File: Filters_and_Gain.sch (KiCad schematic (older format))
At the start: 24 parts, among them U4 OPA388, U5 OPA388, U6 OPA388

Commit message: #4 - Routed board
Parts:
- removed TP18: TestPoint, TestPoint:TestPoint_Pad_D2.0mm, symbol Connector:TestPoint
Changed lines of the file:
@@
 $EndComp
 Connection ~ 5625 3025
-Wire Wire Line
-	5625 1450 5625 1775
 Connection ~ 5625 2300
 Wire Wire Line
@@
 	3175 2200 3575 2200
 $Comp
-L Connector:TestPoint TP18
-U 1 1 5FCA32EA
-P 5625 1775
-F 0 "TP18" V 5579 1963 50  0000 L CNN
-F 1 "TestPoint" V 5670 1963 50  0000 L CNN
-F 2 "TestPoint:TestPoint_Pad_D2.0mm" H 5825 1775 50  0001 C CNN
-F 3 "~" H 5825 1775 50  0001 C CNN
-	1    5625 1775
-	0    1    1    0
-$EndComp
-Connection ~ 5625 1775
-Wire Wire Line
-	5625 1775 5625 2300
-$Comp
 L Device:C C20
 U 1 1 5FCDCCC4
@@
 Wire Wire Line
 	5625 2300 5625 2725
+Wire Wire Line
+	5625 1450 5625 2300
 $EndSCHEMATC

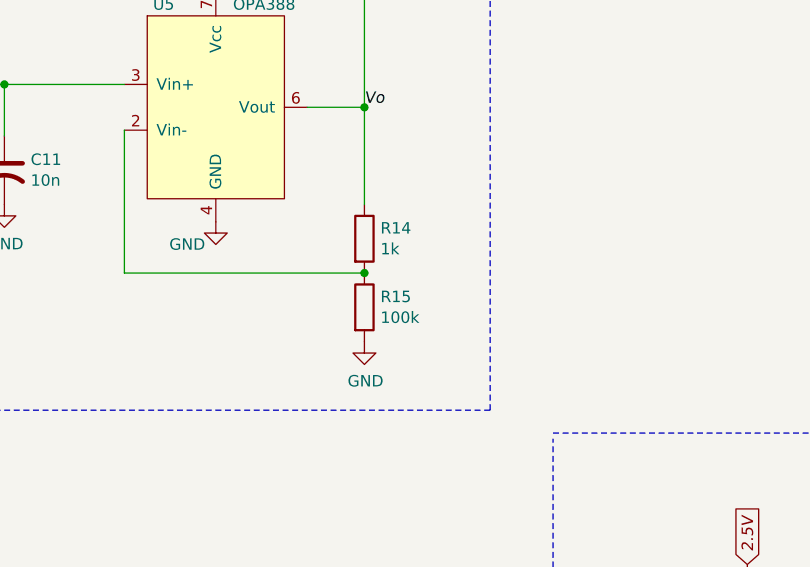
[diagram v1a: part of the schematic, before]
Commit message: #24 - Flip PNP and update low pass filter output resistors
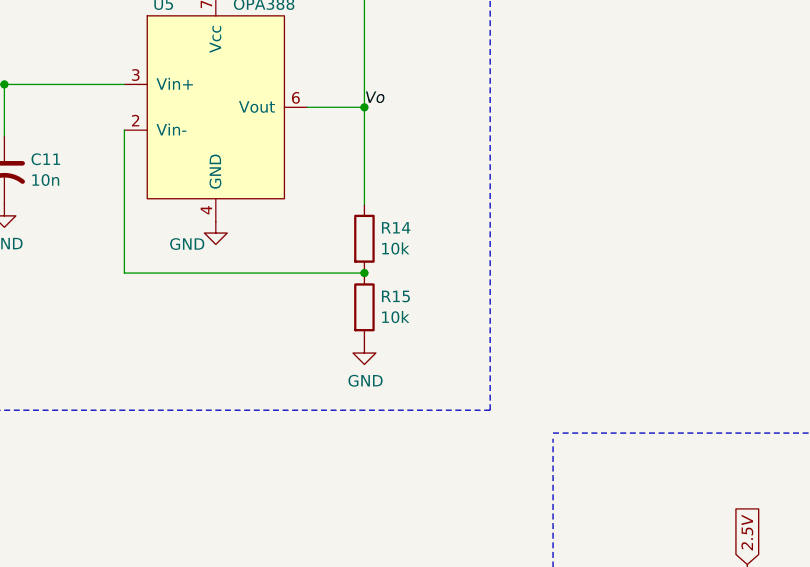
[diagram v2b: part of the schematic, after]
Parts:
- R14: value 1k -> 10k
- R15: value 100k -> 10k
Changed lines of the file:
@@
 P 5625 3175
 F 0 "R15" H 5695 3221 50  0000 L CNN
-F 1 "100k" H 5695 3130 50  0000 L CNN
+F 1 "10k" H 5695 3130 50  0000 L CNN
 F 2 "Resistor_SMD:R_0805_2012Metric_Pad1.20x1.40mm_HandSolder" V 5555 3175 50  0001 C CNN
 F 3 "~" H 5625 3175 50  0001 C CNN
@@
 P 5625 2875
 F 0 "R14" H 5695 2921 50  0000 L CNN
-F 1 "1k" H 5695 2830 50  0000 L CNN
+F 1 "10k" H 5695 2830 50  0000 L CNN
 F 2 "Resistor_SMD:R_0805_2012Metric_Pad1.20x1.40mm_HandSolder" V 5555 2875 50  0001 C CNN
 F 3 "~" H 5625 2875 50  0001 C CNN

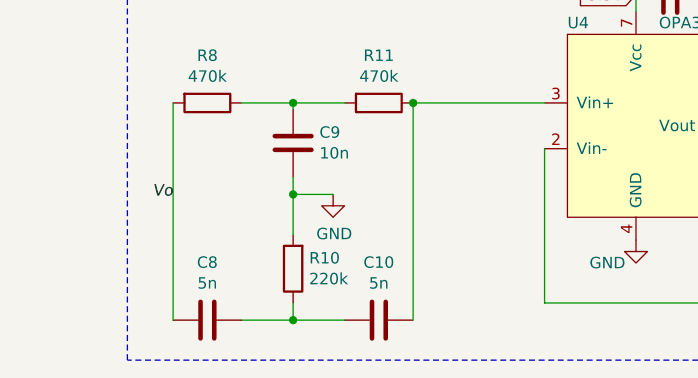
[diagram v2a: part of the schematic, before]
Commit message: Added mounting holes, Added lead-detect to a micro GPIO, and removed requirement that the leads must be attached prior to turning on the device
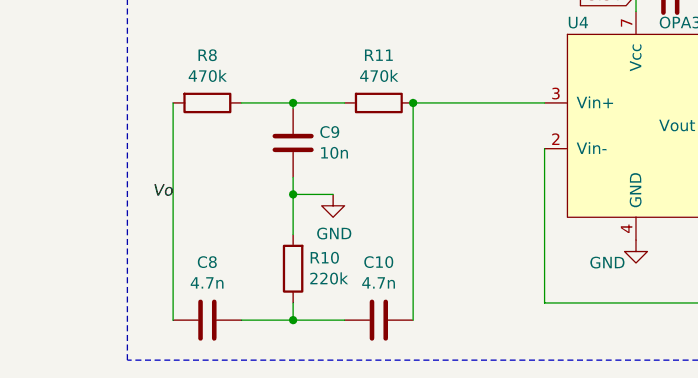
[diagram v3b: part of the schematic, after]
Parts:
- C10, C8: value 5n -> 4.7n
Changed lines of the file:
@@
 P 3200 6000
 F 0 "C10" V 2948 6000 50  0000 C CNN
-F 1 "5n" V 3039 6000 50  0000 C CNN
+F 1 "4.7n" V 3039 6000 50  0000 C CNN
 F 2 "Capacitor_SMD:C_0805_2012Metric_Pad1.18x1.45mm_HandSolder" H 3238 5850 50  0001 C CNN
 F 3 "~" H 3200 6000 50  0001 C CNN
@@
 P 2450 6000
 F 0 "C8" V 2198 6000 50  0000 C CNN
-F 1 "5n" V 2289 6000 50  0000 C CNN
+F 1 "4.7n" V 2289 6000 50  0000 C CNN
 F 2 "Capacitor_SMD:C_0805_2012Metric_Pad1.18x1.45mm_HandSolder" H 2488 5850 50  0001 C CNN
 F 3 "~" H 2450 6000 50  0001 C CNN

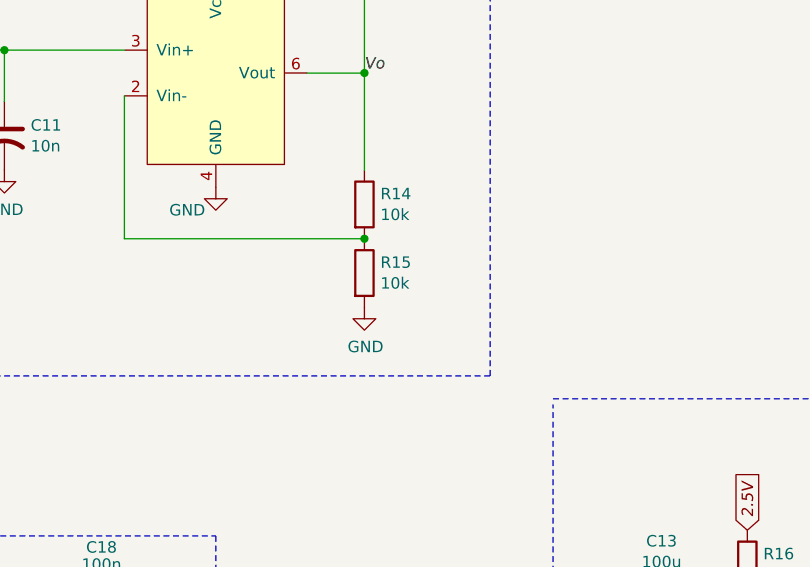
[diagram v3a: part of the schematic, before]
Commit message: #25 - Updated low pass filter. Gain 2x -> 1x. Added ADC divider for battery to account for brand new batteries.
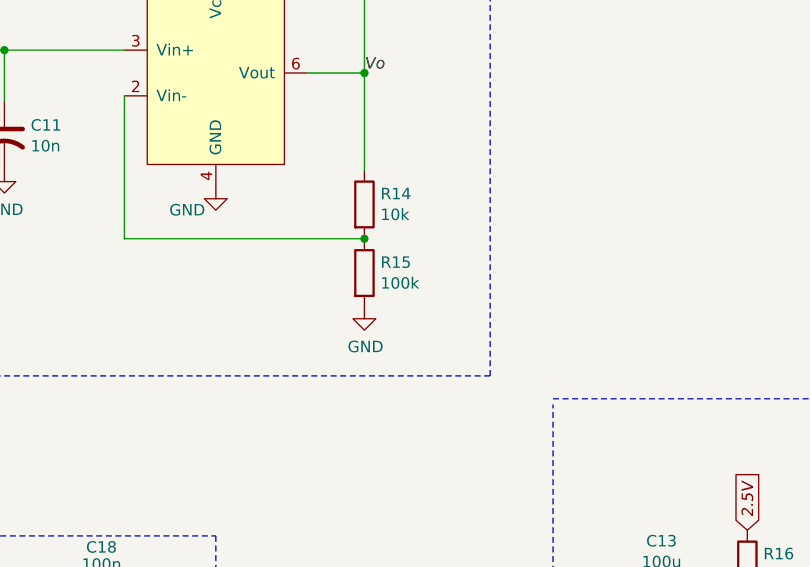
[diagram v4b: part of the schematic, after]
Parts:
- R15: value 10k -> 100k
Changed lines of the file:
@@
 P 5625 3175
 F 0 "R15" H 5695 3221 50  0000 L CNN
-F 1 "10k" H 5695 3130 50  0000 L CNN
+F 1 "100k" H 5695 3130 50  0000 L CNN
 F 2 "Resistor_SMD:R_0805_2012Metric_Pad1.20x1.40mm_HandSolder" V 5555 3175 50  0001 C CNN
 F 3 "~" H 5625 3175 50  0001 C CNN
